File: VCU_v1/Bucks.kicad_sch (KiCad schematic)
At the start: 5 parts, among them U1 TPS5430

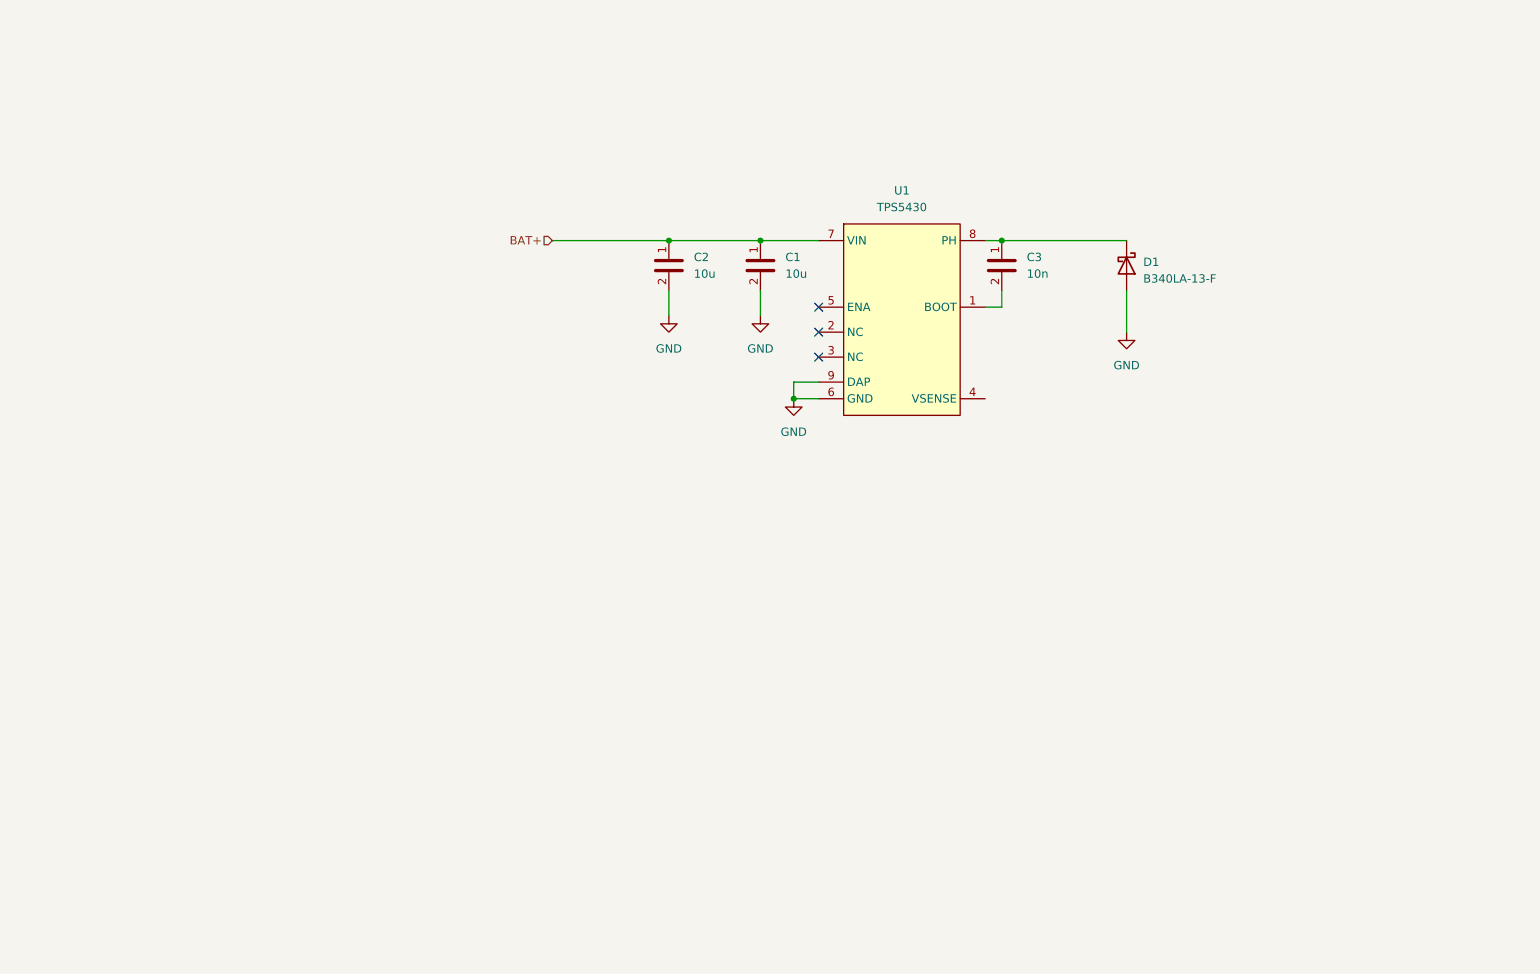
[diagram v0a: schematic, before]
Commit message: finished 12-5 buck
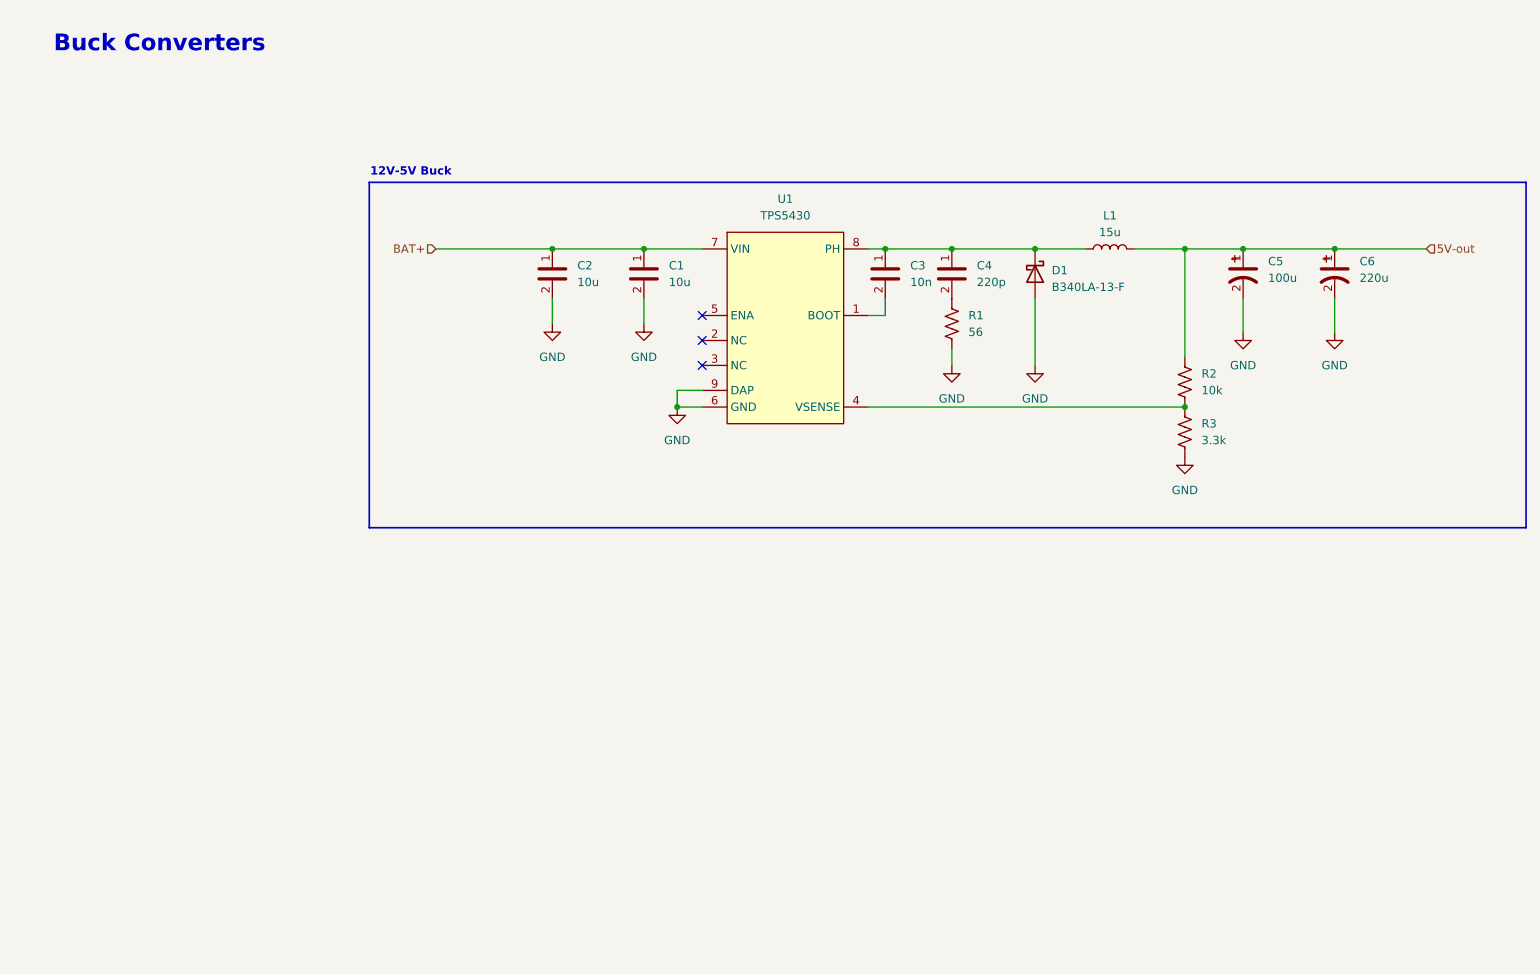
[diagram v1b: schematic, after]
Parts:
- added C4: 220p, Capacitor_SMD:C_0603_1608Metric_Pad1.08x0.95mm_HandSolder, symbol BFR Capacitors:06035C221J4Z2A
- added C5: 100u, Capacitor_THT:CP_Radial_D8.0mm_P3.50mm, symbol BFR Capacitors:50ZLH100MEFC8X11.5
- added C6: 220u, Capacitor_THT:CP_Radial_D8.0mm_P3.50mm, symbol BFR Capacitors:35ZLH220MEFC8X11.5
- added L1: 15u, symbol Device:L
- added R1: 56, Resistor_SMD:R_0603_1608Metric_Pad0.98x0.95mm_HandSolder, symbol BFR Resistors:RMCF0603FT56R0
- added R2: 10k, Resistor_SMD:R_0603_1608Metric_Pad0.98x0.95mm_HandSolder, symbol BFR Resistors:RMCF0603FT10K0
- added R3: 3.3k, Resistor_SMD:R_0603_1608Metric_Pad0.98x0.95mm_HandSolder, symbol BFR Resistors:RMCF0603FT3K30
- U1: Digikey P/N (none) -> 296-26988-1-ND; Manufacturer (none) -> Texas Instruments; Manufacturer P/N (none) -> TPS5430DDAR; Mouser P/N (none) -> 595-TPS5430DDAR
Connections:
- net GND: now also C5.2, C6.2, R1.2, R3.2
- net at C3.1, D1.1 (K), U1.8 (PH): now also C4.1, L1.1
- net at U1.4 (VSENSE): now also R2.1, R3.1
- new net: C4.2, R1.1
- new net 5V-out: C5.1, C6.1, L1.2, R2.2
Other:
- note added: "12V-5V Buck"
- note added: "Buck Converters"
- moved on the sheet: C1, C2, C3, D1, U1

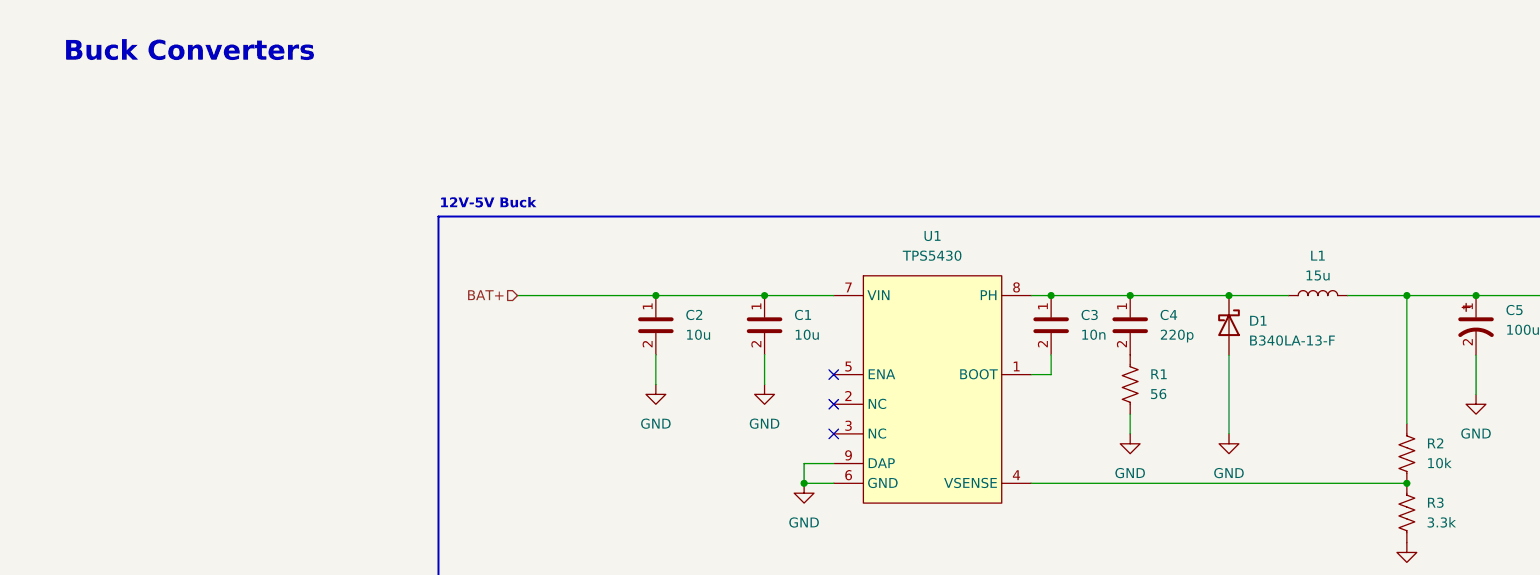
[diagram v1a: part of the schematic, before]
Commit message: added STM, broke out communications I/Os for CAN, SPI, ADC
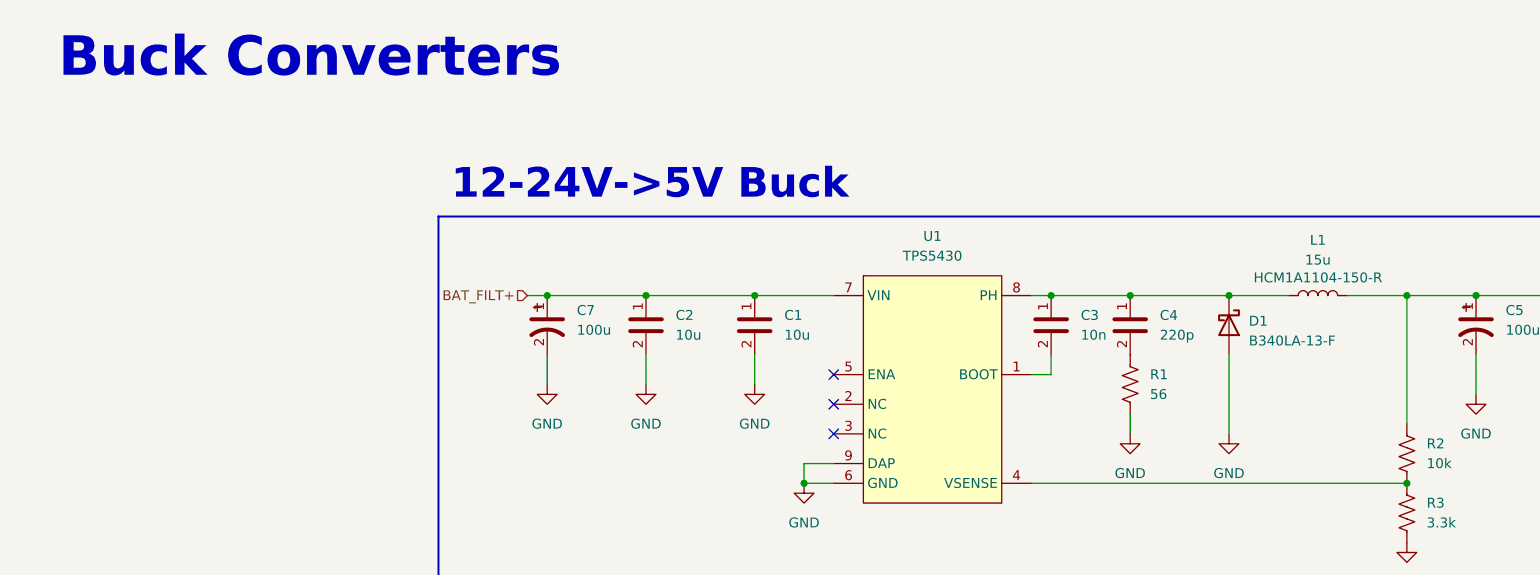
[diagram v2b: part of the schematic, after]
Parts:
- added C7: 100u, Capacitor_THT:CP_Radial_D8.0mm_P3.50mm, symbol BFR Capacitors:50ZLH100MEFC8X11.5
- L1: Mouser P/N (none) -> 704-HCM1A1104-150-R; P/N (none) -> HCM1A1104-150-R
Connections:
- net GND: now also C7.2
- net BAT+ renamed BAT_FILT+
- net BAT_FILT+: now also C7.1
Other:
- note added: "12-24V->5V Buck"
- note removed: "12V-5V Buck"
- moved on the sheet: C1, C2

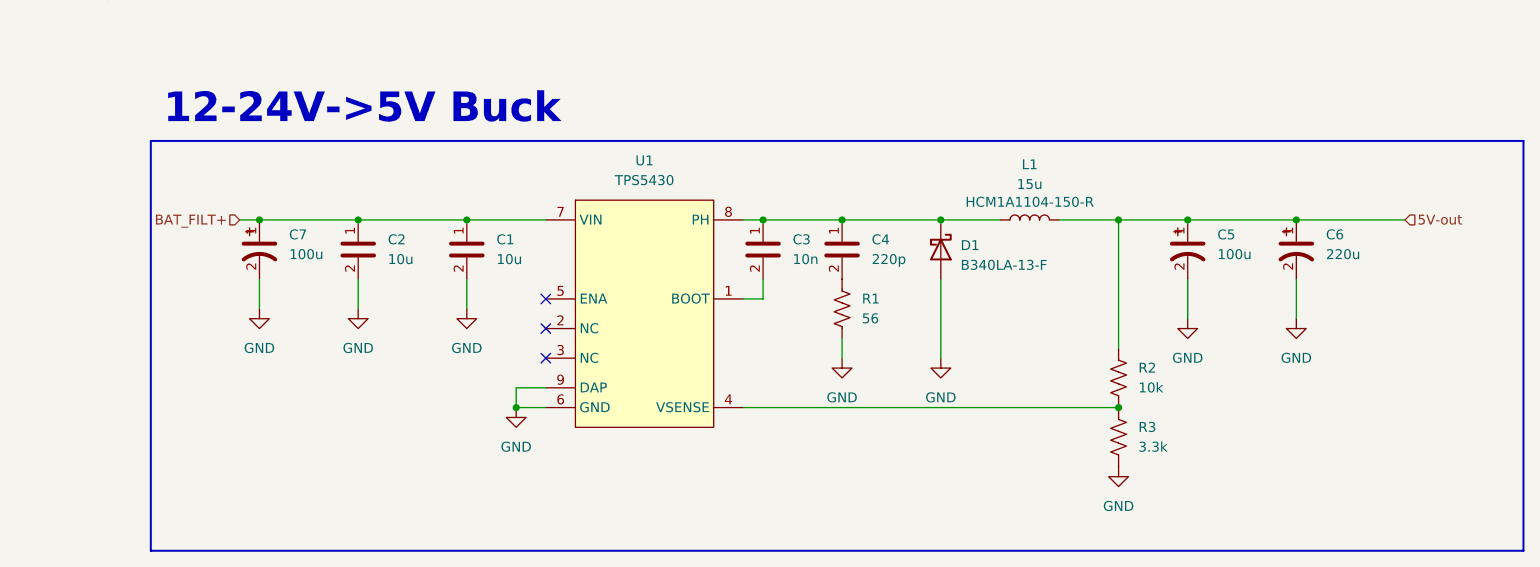
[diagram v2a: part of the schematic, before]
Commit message: added rpp, pedal buffer/low pass, can transceivers, began connector pinout
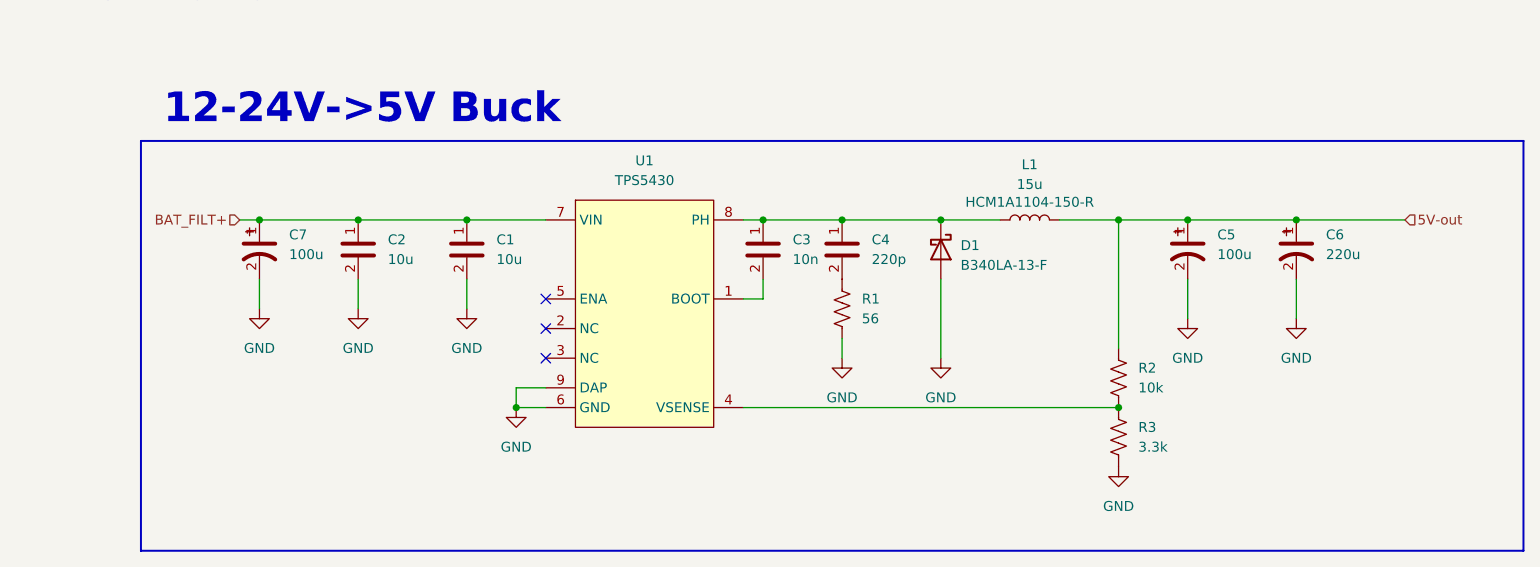
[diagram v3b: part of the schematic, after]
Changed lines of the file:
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@@
 	(paper "A4")
 	(rectangle
-		(start 62.23 38.1)
+		(start 60.96 38.1)
 		(end 238.76 90.805)
 		(stroke

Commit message: p dih r
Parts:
- added C52, C60: 100u, Capacitor_THT:CP_Radial_D8.0mm_P3.50mm, symbol BFR Capacitors:50ZLH100MEFC8X11.5
- added C56, C57: 10u, Capacitor_SMD:C_0603_1608Metric_Pad1.08x0.95mm_HandSolder, symbol BFR Capacitors:CL10A106KP8NNNC
- added C58: 10n, Capacitor_SMD:C_0603_1608Metric_Pad1.08x0.95mm_HandSolder, symbol BFR Capacitors:VJ0603Y103KXAAC
- added C59: 220p, Capacitor_SMD:C_0603_1608Metric_Pad1.08x0.95mm_HandSolder, symbol BFR Capacitors:06035C221J4Z2A
- added C61: 220u, Capacitor_THT:CP_Radial_D8.0mm_P3.50mm, symbol BFR Capacitors:35ZLH220MEFC8X11.5
- added D6: B340LA-13-F, Diode_SMD:D_SMA_Handsoldering, symbol .Diode-Schottky:B340LA-13-F
- added L2: 33u, symbol Device:L
- added R51: 56, Resistor_SMD:R_0603_1608Metric_Pad0.98x0.95mm_HandSolder, symbol BFR Resistors:RMCF0603FT56R0
- added R52: 10k, Resistor_SMD:R_0603_1608Metric_Pad0.98x0.95mm_HandSolder, symbol BFR Resistors:RMCF0603FT10K0
- added R53: 620, Resistor_SMD:R_0603_1608Metric_Pad0.98x0.95mm_HandSolder, symbol BFR Resistors:RMCF0603FT620R
- added U17: TPS5430, symbol TPS5430:TPS5430
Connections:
- net BAT_FILT+: now also C52.1, C56.1, C57.1, U17.7 (VIN)
- net GND: now also C52.2, C56.2, C57.2, C60.2, C61.2, D6.2 (A), R51.2, R53.1, U17.6 (GND), U17.9 (DAP)
- new net: C58.1, C59.1, D6.1 (K), L2.1, U17.8 (PH)
- new net: C58.2, U17.1 (BOOT)
- new net: R52.1, R53.2, U17.4 (VSENSE)
- new net: C59.2, R51.1
- new net 20V-out: C60.1, C61.1, L2.2, R52.2
- no-connect marks 3 -> 6
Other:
- note added: "24V-20V Buck"

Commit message: left to do before layout: wire DRS/Debug LEDs to connector, add BRUHbus ports
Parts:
- removed C61: 220u, Capacitor_THT:CP_Radial_D8.0mm_P3.50mm, symbol BFR Capacitors:35ZLH220MEFC8X11.5
- C60: value 100u -> 150u; Digikey P/N P12392-ND -> (none); Mouser P/N 667-EEU-FM1H101 -> 667-EEU-FM1V151B; Pretty Name 100uF 50V Through-hole Capacitor -> (none)
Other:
- moved on the sheet: C60
